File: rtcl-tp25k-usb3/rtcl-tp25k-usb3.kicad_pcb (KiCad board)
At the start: 4 copper layers, 80 x 35 mm, 103 parts, among them J1 ZX360D-B-10P(30), J10 SSQ-106-02-F-D-RA, J2 0525592253, J3 DF40C(2.0)-60DS-0.4V(51), J4 DF40C(2.0)-60DS-0.4V(51), J5 JTAG, J6 Conn_01x02, J7 Conn_01x03, Q2 NTK3134NT1G, Q3 NTK3134NT1G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

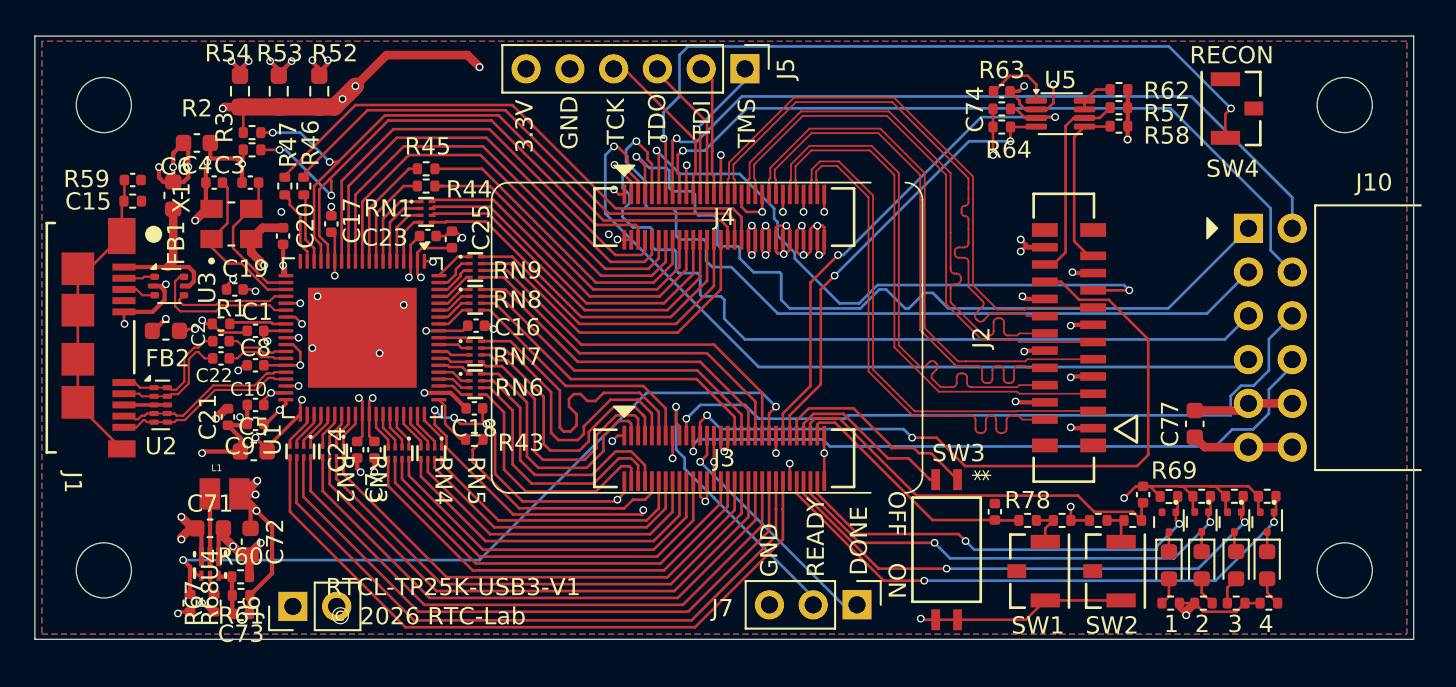
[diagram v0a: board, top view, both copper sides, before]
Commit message: Update selection filter settings in KiCad project file
- Changed selection filter options to enable visibility for dimensions, footprints, graphics, keepouts, locked items, other items, pads, text, vias, and zones.
- This enhances the usability of the design environment by allowing more elements to be selected and manipulated.
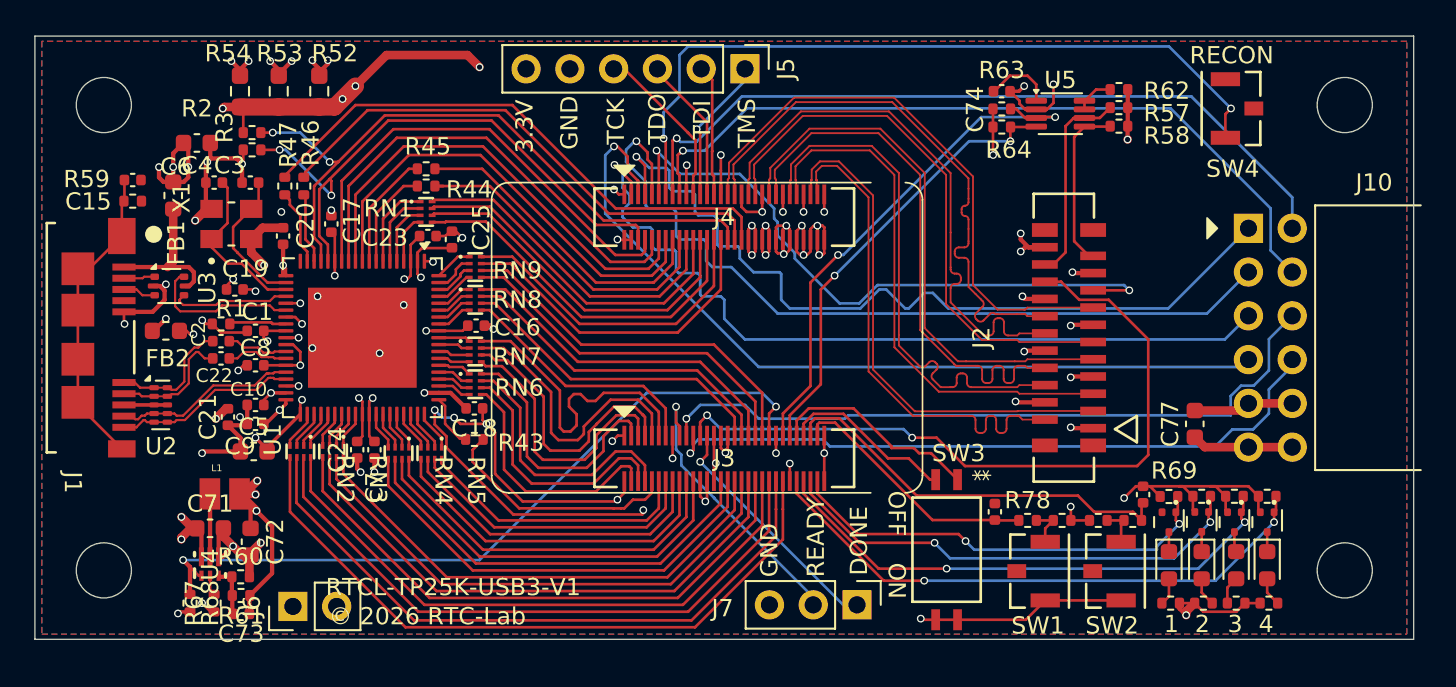
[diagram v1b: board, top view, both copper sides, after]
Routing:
- net +2V5: track 46.1 -> 46.7 mm
- net VCC: vias 16 -> 15
- added copper zone on In2.Cu, net +3V3
- added copper zone on In2.Cu, net VCC

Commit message: WIP
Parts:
- J10: footprint rtcl-p25k-usb3:PMOD_02x06_2.54mm -> rtcl-tp25k-usb3:PMOD_02x06_2.54mm
- L1: footprint rtcl-p25k-usb3:INDC2016X100N -> rtcl-tp25k-usb3:INDC2016X100N
- RN1, RN2, RN3, RN4, RN5, RN6, RN7, RN8, RN9: footprint rtcl-p25k-usb3:RES_YC104_YAG -> rtcl-tp25k-usb3:RES_YC104_YAG
- U4: footprint rtcl-p25k-usb3:DMQ0006A -> rtcl-tp25k-usb3:DMQ0006A
- X1: footprint rtcl-p25k-usb3:XTAL_ABM8-30.000MHz-D1X-T -> rtcl-tp25k-usb3:XTAL_ABM8-30.000MHz-D1X-T

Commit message: DRCは通した
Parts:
- J1: footprint rtcl-p25k-usb3:CONN10_ZX360D-B-10P30_HIR -> rtcl-tp25k-usb3:CONN10_ZX360D-B-10P30_HIR
- J2: footprint rtcl-p25k-usb3:CON_525592253_MOL -> rtcl-tp25k-usb3:CON_525592253_MOL
- J3, J4: footprint rtcl-p25k-usb3:CONN_DF40C-60DS_HIR -> rtcl-tp25k-usb3:CONN_DF40C-60DS_HIR
- moved R69 0.21 mm to (175.8, 109.0)
- moved R72 0.20 mm to (177.7, 109.0)
- moved R74 0.20 mm to (179.6, 109.0)
- moved R76 0.20 mm to (181.5, 109.0)
- moved R60 0.06 mm to (122.0, 113.9)
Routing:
- net GND: track 148.3 -> 147.0 mm

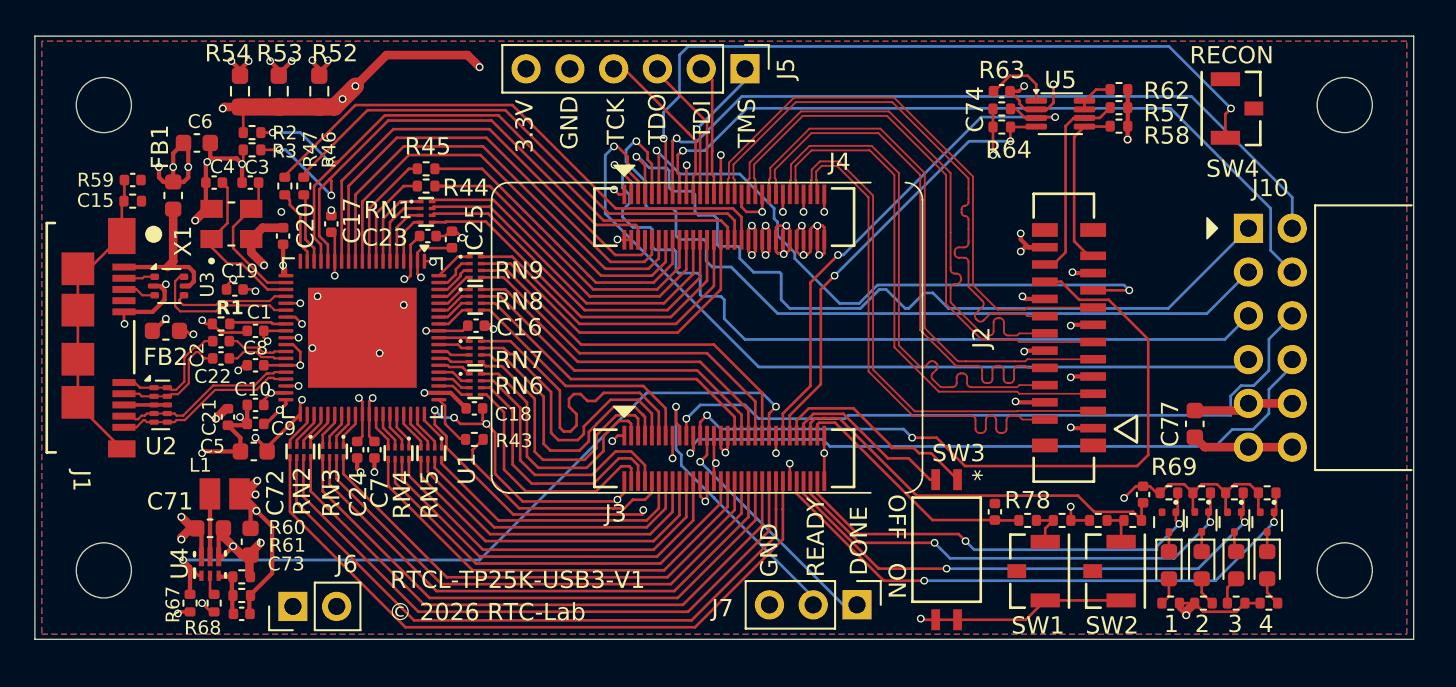
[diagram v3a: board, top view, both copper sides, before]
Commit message: PMOD配線長調整
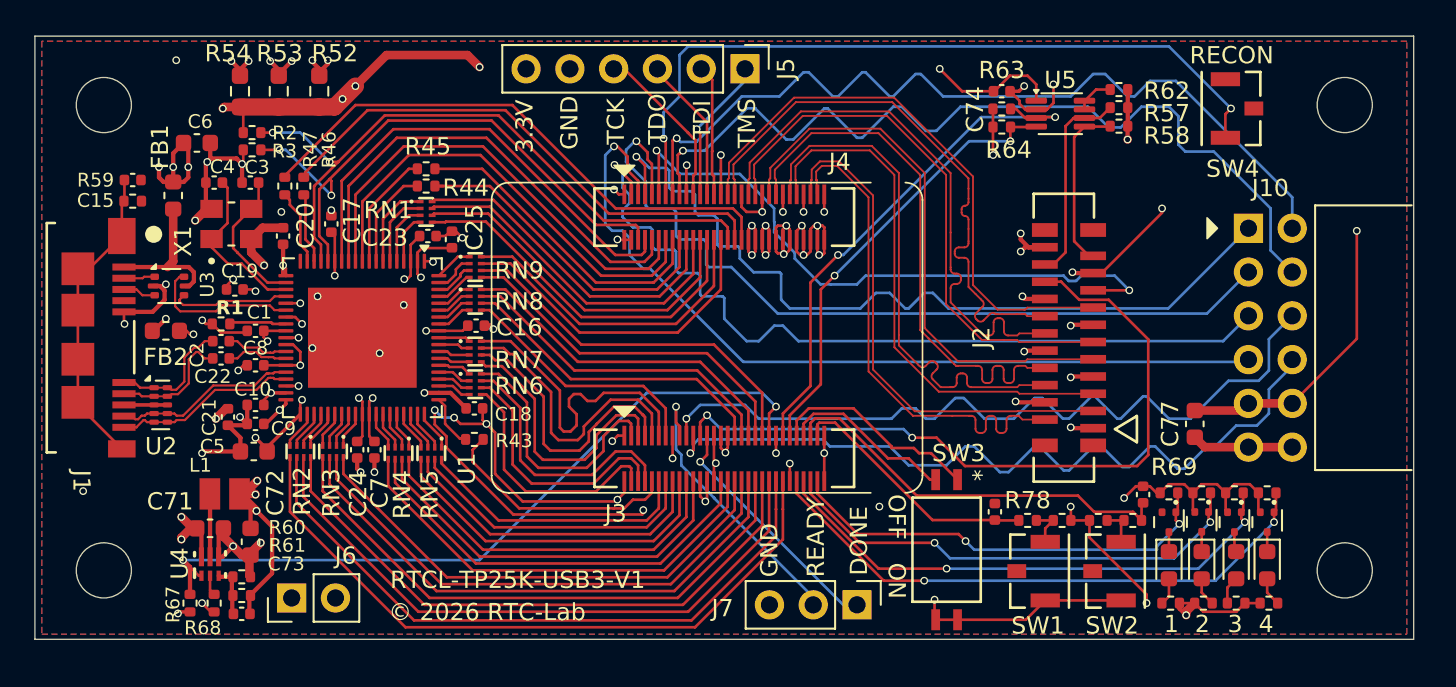
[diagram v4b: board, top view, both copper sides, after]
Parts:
- moved J6 0.49 mm to (124.9, 115.1)
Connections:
- C77 pad 1: VCCIO33 -> +3V3
- J10 pad 11: VCCIO33 -> +3V3
- J10 pad 12: VCCIO33 -> +3V3
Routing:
- net GND: track 147.0 -> 198.9 mm, vias 54 -> 61
- net +3V3: track 207.9 -> 258.2 mm
- net /D1_IOB14B_40P: track 44.7 -> 50.8 mm
- net VCCIO33: track 5.89 -> 0.00 mm
- net /C3_IOB56B_UART_TX: track 39.8 -> 45.2 mm
- net /E1_IOB12B_40P: track 44.7 -> 49.9 mm
- net /B3_IOB56A_UART_RX: track 41.0 -> 45.0 mm
- net /B2_IOB4A_40P: track 48.0 -> 48.9 mm
- net /C2_IOB4B_40P: track 48.8 -> 49.5 mm
- net VCC: track 193.8 -> 193.3 mm

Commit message: Update KiCad project settings and add length table for Tang Primer 25K
- Changed active layer from 2 to 4 in the KiCad project file.
- Updated selection filter to enable visibility for dimensions, footprints, graphics, keepouts, other items, pads, text, vias, and zones.
- Modified visible layers and zone display mode in the KiCad project file.
- Added a new Excel file for the Tang Primer 25K length table in the documentation directory.
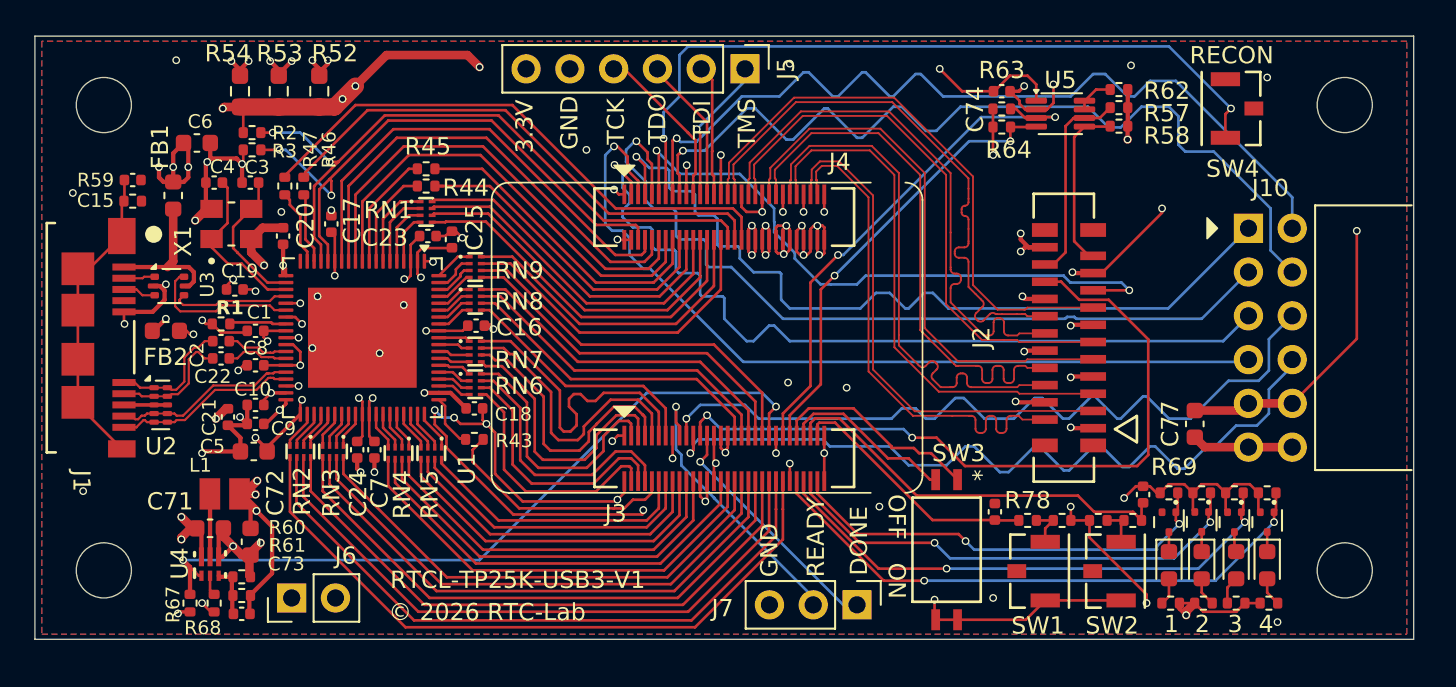
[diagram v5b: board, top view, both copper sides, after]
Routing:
- net GND: track 198.9 -> 281.1 mm, vias 61 -> 70

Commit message: WIP
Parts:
- added R81: 4.7k, Resistor_SMD:R_0402_1005Metric, F.Cu at (175.1, 97.3)
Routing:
- net /A1_IOB24A_40P: track 36.9 -> 38.0 mm
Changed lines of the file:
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@@
 		)
 	)
+	(footprint "Resistor_SMD:R_0402_1005Metric"
+		(layer "F.Cu")
+		(at 175.1 97.3)
+		(descr "Resistor SMD 0402 (1005 Metric), square (rectangular) end terminal, IPC-7351 nominal, (Body size source: IPC-SM-782 page 72, https://www.pcb-3d.com/wordpress/wp-content/uploads/ipc-sm-782a_amendment_1_and_2.pdf)")
+		(tags "resistor")
+		(property "Reference" "R81"
+			(at 0 -1.17 0)
+			(layer "F.SilkS")
+			(effects
+				(font
+					(size 1 1)
+					(thickness 0.15)
+				)
+			)
+		)
+		(property "Value" "4.7k"
+			(at 0 1.17 0)
+			(layer "F.Fab")
+			(effects
+				(font
+					(size 1 1)
+					(thickness 0.15)
+				)
+			)
+		)
+		(property "Datasheet" ""
+			(at 0 0 0)
+			(layer "F.Fab")
+			(hide yes)
+			(effects
+				(font
+					(size 1.27 1.27)
+				)
+			)
+		)
+		(property "Description" "Resistor"
+			(at 0 0 0)
+			(layer "F.Fab")
+			(hide yes)
+			(effects
+				(font
+					(size 1.27 1.27)
+				)
+			)
+		)
+		(property "KiLib_Generator" "SMD_2terminal_chip_molded"
+			(at 0 0 0)
+			(layer "F.SilkS")
+			(hide yes)
+			(effects
+				(font
+					(size 1 1)
+					(thickness 0.15)
+				)
+			)
+		)
+		(property ki_fp_filters "R_*")
+		(sheetname "/")
+		(sheetfile "rtcl-tp25k-usb3.kicad_sch")
+		(units
+			(unit
+				(name "A")
+				(pins "1" "2")
+			)
+		)
+		(attr smd)
+		(duplicate_pad_numbers_are_jumpers no)
+		(fp_line
+			(start -0.153641 -0.38)
+			(end 0.153641 -0.38)
+			(stroke
+				(width 0.12)
+				(type solid)
+			)
+			(layer "F.SilkS")
+		)
+		(fp_line
+			(start -0.153641 0.38)
+			(end 0.153641 0.38)
+			(stroke
+				(width 0.12)
+				(type solid)
+			)
+			(layer "F.SilkS")
+		)
+		(fp_rect
+			(start -0.93 -0.47)
+			(end 0.93 0.47)
+			(stroke
+				(width 0.05)
+				(type solid)
+			)
+			(fill no)
+			(layer "F.CrtYd")
+		)
+		(fp_rect
+			(start -0.525 -0.27)
+			(end 0.525 0.27)
+			(stroke
+				(width 0.1)
+				(type solid)
+			)
+			(fill no)
+			(layer "F.Fab")
+		)
+		(fp_text user "${REFERENCE}"
+			(at 0 0 0)
+			(layer "F.Fab")
+			(effects
+				(font
+					(size 0.26 0.26)
+					(thickness 0.04)
+				)
+			)
+		)
+		(pad "1" smd roundrect
+			(at -0.51 0)
+			(size 0.54 0.64)
+			(layers "F.Cu" "F.Mask" "F.Paste")
+			(roundrect_rratio 0.25)
+			(net "/A1_IOB24A_40P")
+			(pintype "passive")
+		)
+		(pad "2" smd roundrect
+			(at 0.51 0)
+			(size 0.54 0.64)
+			(layers "F.Cu" "F.Mask" "F.Paste")
+			(roundrect_rratio 0.25)
+			(net "GND")
+			(pintype "passive")
+		)
+		(embedded_fonts no)
+		(model "${KICAD10_3DMODEL_DIR}/Resistor_SMD.3dshapes/R_0402_1005Metric.step"
+			(offset
+				(xyz 0 0 0)
+			)
+			(scale
+				(xyz 1 1 1)
+			)
+			(rotate
+				(xyz 0 0 0)
+			)
+		)
+	)
 	(footprint "rtcl-tp25k-usb3:RES_YC104_YAG"
 		(layer "F.Cu")
@@
 		(width 0.156464)
 		(layer "F.Cu")
+		(net "/A1_IOB24A_40P")
+	)
+	(segment
+		(start 174.59 97.3)
+		(end 173.550011 97.3)
+		(width 0.156464)
+		(layer "F.Cu")
+		(net "/A1_IOB24A_40P")
+	)
+	(segment
+		(start 173.550011 97.3)
+		(end 173.5 97.249989)
+		(width 0.156464)
+		(layer "F.Cu")

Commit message: WIP
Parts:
- added C75: 0.1uF, Capacitor_SMD:C_0402_1005Metric, F.Cu at (172.9, 88.8)
- added C76: 0.1uF, Capacitor_SMD:C_0402_1005Metric, F.Cu at (172.9, 84.6)
- added Q6: NTK3134NT1G, Package_TO_SOT_SMD:SOT-723, F.Cu at (117.5, 109.5)
- added R82: 4.7k, Resistor_SMD:R_0402_1005Metric, F.Cu at (118.2, 113.2)
- J2: value 0525592253 -> CF20221V0R0-NH
- moved R68 7.55 mm to (117.5, 108.0), turned to 0 degrees
- moved L1 0.41 mm to (120.6, 109.1)
- moved R60 0.20 mm to (122.2, 113.9)
- moved U4 0.17 mm to (120.0, 113.1)
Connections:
- R63 pad 1: +3.3VP -> VCC
- R64 pad 1: +3.3VP -> VCC
- R68 pad 1: /G10_IOT7B -> VCC
- R68 pad 2: GND -> /G10_IOT7B
- U4 pad 1: /G10_IOT7B -> Net-(Q6-D)
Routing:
- net VCC: track 193.3 -> 230.5 mm, vias 15 -> 17
- net Net-(Q6-D): track 0.00 -> 5.24 mm
- net GND: track 281.1 -> 276.7 mm
- net +3.3VP: track 87.4 -> 83.0 mm, vias 7 -> 6
- net /G10_IOT7B: track 43.6 -> 41.4 mm
- net +5V: track 135.2 -> 136.6 mm
- net Net-(U5-EN): track 2.26 -> 3.27 mm
- net Net-(U4-SW): track 3.65 -> 4.17 mm

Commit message: WIP
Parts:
- added R83: 4.7k, Resistor_SMD:R_0402_1005Metric, F.Cu at (175.2, 98.5)
- moved R68 0.20 mm to (117.5, 107.8)
- moved R81 0.10 mm to (175.2, 97.3)
- moved C72 0.10 mm to (122.6, 111.8)
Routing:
- net /E3_IOB60A_40P: track 42.5 -> 44.2 mm
- net GND: track 276.7 -> 278.1 mm
